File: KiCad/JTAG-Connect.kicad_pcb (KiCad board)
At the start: 2 copper layers, 16.5 x 21 mm, 2 parts, among them J1 Conn_02x05_Odd_Even, J2 Conn_02x03_Odd_Even

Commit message: updated design
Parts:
- added J3: Conn_02x05_Odd_Even, JTAG-Connect:PinHeader_2x05_P2.00mm_JTAG_connect_on_SMD_pads, F.Cu at (130.5, 74.0)
- added J4: Conn_02x05_Odd_Even, Connector_IDC:IDC-Header_2x05_P2.54mm_Vertical, F.Cu at (139.5, 64.9)
- added J5: Conn_02x03_Odd_Even, JTAG-Connect:PinHeader_2x03_P2.00mm_JTAG_connect_on_SMD_pads, F.Cu at (161.5, 72.0)
- added J6: Conn_02x03_Odd_Even, JTAG-Connect:PinHeader_2x03_P2.00mm_JTAG_connect_on_SMD_pads, F.Cu at (180.5, 72.0)
- added REF**: OSHW-Logo2_9.8x8mm_Copper, Symbol:OSHW-Logo2_9.8x8mm_Copper, F.Cu at (171.0, 70.0)
- added REF**: OSHW-Logo2_9.8x8mm_Copper, Symbol:OSHW-Logo2_9.8x8mm_Copper, F.Cu at (121.0, 69.8)
- J2: value Conn_02x03_Odd_Even -> Conn_02x05_Odd_Even; footprint Connector_PinHeader_2.00mm:PinHeader_2x03_P2.00mm_Vertical -> JTAG-Connect:PinHeader_2x05_P2.00mm_JTAG_connect_on_SMD_pads
- moved J1 15.2 mm to (89.5, 64.9), turned to 0 degrees
- moved J2 13.8 mm to (111.5, 74.0)
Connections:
- J2 pad 4: TDI -> Vtarget
- J2 pad 6: Vtarget -> Net-(J2-Pad6)
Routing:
- net TCK2: track 0.00 -> 38.7 mm
- net TDO2: track 0.00 -> 33.7 mm
- net TDI: track 8.10 -> 41.5 mm
- net TCK: track 13.0 -> 39.1 mm
- net TMS2: track 0.00 -> 25.7 mm
- net TDO: track 9.05 -> 34.2 mm
- net TMS: track 8.83 -> 30.7 mm
- net TDI2: track 0.00 -> 21.1 mm
- net Vtarget2: track 0.00 -> 16.7 mm
- net Vtarget: track 25.1 -> 18.3 mm
- net GND: vias 0 -> 2
- added copper zone on B.Cu, net (none)
- added copper zone on F.Cu, net (none)
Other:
- board size 16.5 x 21 mm -> 100 x 100 mm
- board text added: "GND"
- board text added: "JLCJLCJLCJLC"
- board text added: "JTAG-connect"
- board text added: "NC"
- board text added: "TCK"
- board text added: "TDI"
- board text added: "TDO"
- board text added: "TMS"
- board text added: "V-CUT"
- board text added: "Vtarget"

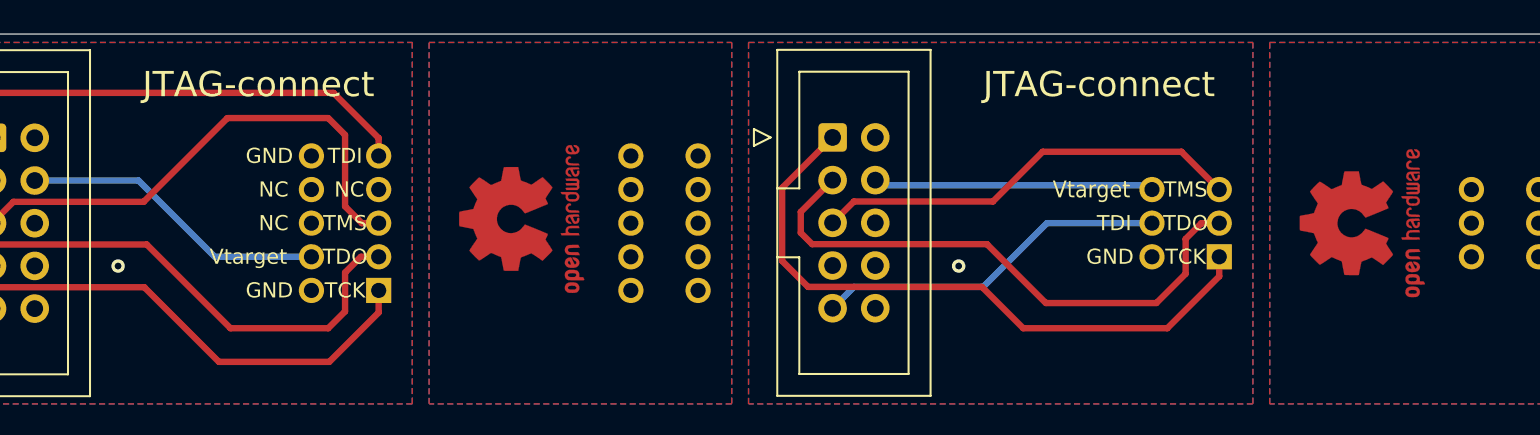
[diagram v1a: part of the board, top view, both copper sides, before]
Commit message: Increased OSHW-symbol text size
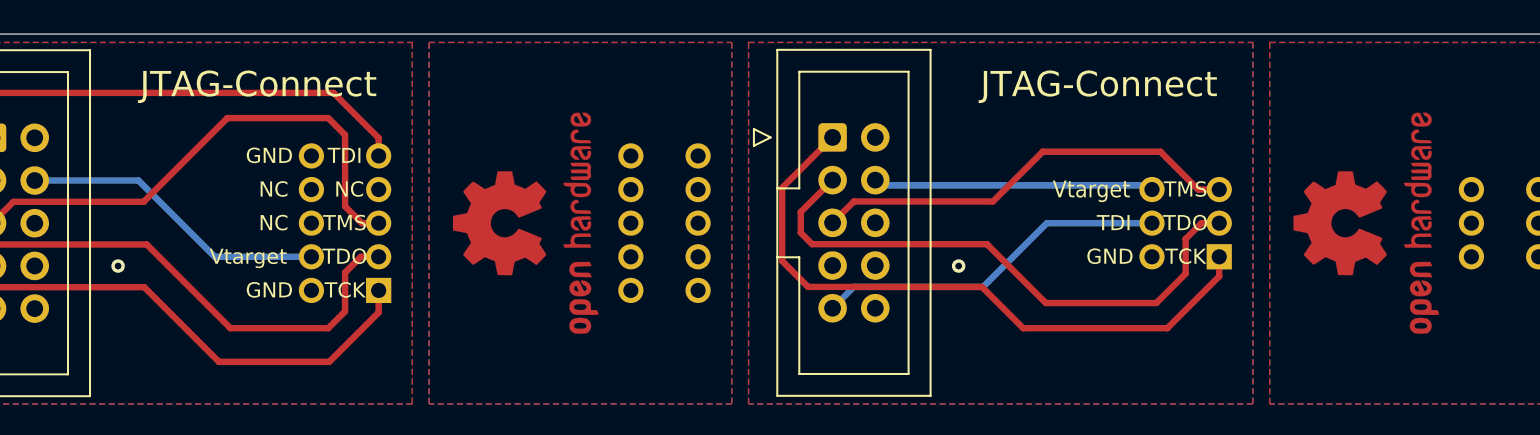
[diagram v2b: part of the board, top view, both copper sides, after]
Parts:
- moved REF** 0.25 mm to (121.0, 70.0)
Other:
- board text added: "JTAG-Connect"
- board text removed: "JTAG-connect"

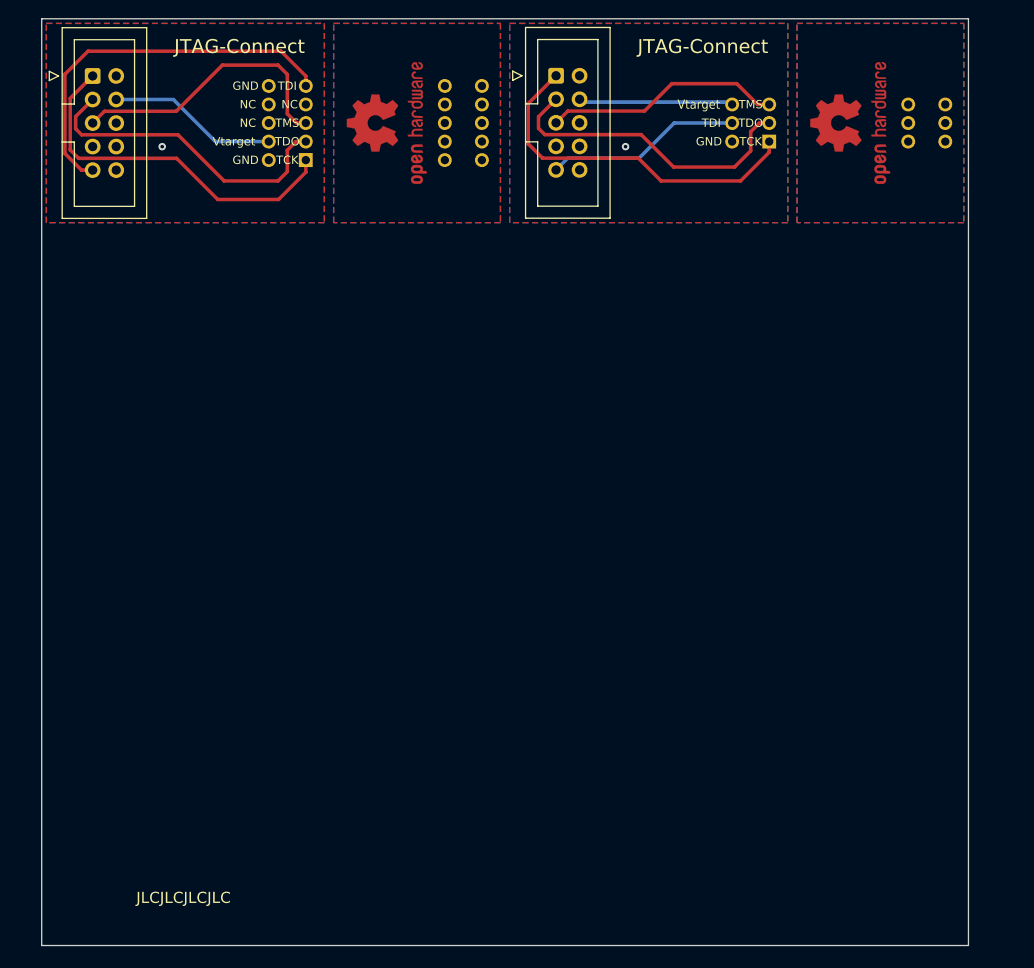
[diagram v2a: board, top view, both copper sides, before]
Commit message: Updated design to fit DIY spring clip.
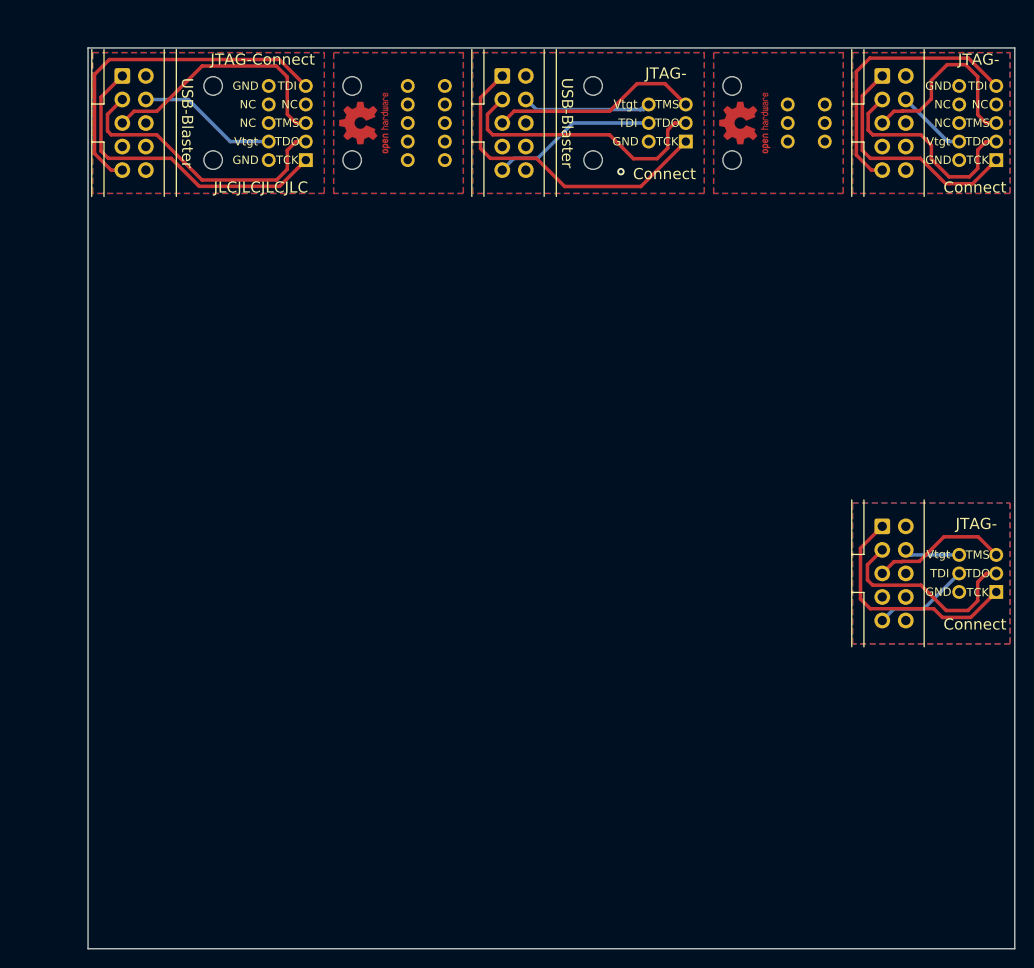
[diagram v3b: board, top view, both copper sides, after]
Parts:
- removed the REF** at (121.0, 70.0)
- removed the REF** at (171.0, 70.0)
- added H1: MountingHole, MountingHole:MountingHole_2mm, F.Cu at (102.5, 66.0)
- added H2: MountingHole, MountingHole:MountingHole_2mm, F.Cu at (102.5, 74.0)
- added H3: MountingHole, MountingHole:MountingHole_2mm, F.Cu at (117.5, 66.0)
- added H4: MountingHole, MountingHole:MountingHole_2mm, F.Cu at (117.5, 74.0)
- added H5: MountingHole, MountingHole:MountingHole_2mm, F.Cu at (143.5, 66.0)
- added H6: MountingHole, MountingHole:MountingHole_2mm, F.Cu at (143.5, 74.0)
- added H7: MountingHole, MountingHole:MountingHole_2mm, F.Cu at (158.5, 74.0)
- added H8: MountingHole, MountingHole:MountingHole_2mm, F.Cu at (158.5, 66.0)
- added J10: Conn_02x03_Odd_Even, JTAG-Connect:PinHeader_2x03_P2.00mm_JTAG_connect_on_SMD_pads, F.Cu at (186.0, 120.6)
- added J7: Conn_02x05_Odd_Even, Connector_IDC:IDC-Header_2x05_P2.54mm_Vertical, F.Cu at (174.7, 64.9)
- added J8: Conn_02x05_Odd_Even, JTAG-Connect:PinHeader_2x05_P2.00mm_JTAG_connect_on_SMD_pads, F.Cu at (186.0, 74.0)
- added J9: Conn_02x05_Odd_Even, Connector_IDC:IDC-Header_2x05_P2.54mm_Vertical, F.Cu at (174.7, 113.5)
- added REF**: OSHW-Logo2_7.3x6mm_Copper, Symbol:OSHW-Logo2_7.3x6mm_Copper, F.Cu at (159.8, 70.0)
- added REF**: OSHW-Logo2_7.3x6mm_Copper, Symbol:OSHW-Logo2_7.3x6mm_Copper, F.Cu at (118.8, 70.0)
- moved J6 13.0 mm to (167.5, 72.0)
- moved J5 9.00 mm to (152.5, 72.0)
- moved J4 5.80 mm to (133.7, 64.9)
- moved J3 4.00 mm to (126.5, 74.0)
- moved J1 3.20 mm to (92.7, 64.9)
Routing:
- net TDI3: track 0.00 -> 29.4 mm
- net TCK3: track 0.00 -> 25.9 mm
- net TCK4: track 0.00 -> 25.4 mm
- net TDO3: track 0.00 -> 23.5 mm
- net TDO4: track 0.00 -> 22.0 mm
- net TMS3: track 0.00 -> 21.1 mm
- net TMS4: track 0.00 -> 14.7 mm
- net TDI4: track 0.00 -> 10.4 mm
- net Vtarget3: track 0.00 -> 7.64 mm
- net Vtarget4: track 0.00 -> 5.98 mm
- net TCK: track 39.1 -> 33.9 mm
- net TDI: track 41.5 -> 36.9 mm
- net TDO2: track 33.7 -> 29.3 mm
- net TCK2: track 38.7 -> 34.7 mm
- net TDO: track 34.2 -> 30.6 mm
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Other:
- board size 100 x 100 mm -> 100 x 97.2 mm
- board text added: "Connect"
- board text added: "JTAG-"
- board text added: "USB-Blaster"
- board text added: "Vtgt"
- board text removed: "Vtarget"
